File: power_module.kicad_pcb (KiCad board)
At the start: 4 copper layers, 95 x 66 mm, 71 parts, among them J1 USB_C_PD, J2 OUTPUT, J3 I2C_BREAKOUT, Q1 DUAL_N_FET, Q2 DUAL_N_FET, Q3 DUAL_N_FET, Q4 DUAL_N_FET, SW1 ON_OFF, U1 BQ7692003, U2 CH224K, U3 BQ24650, U4 LM5176PWPR

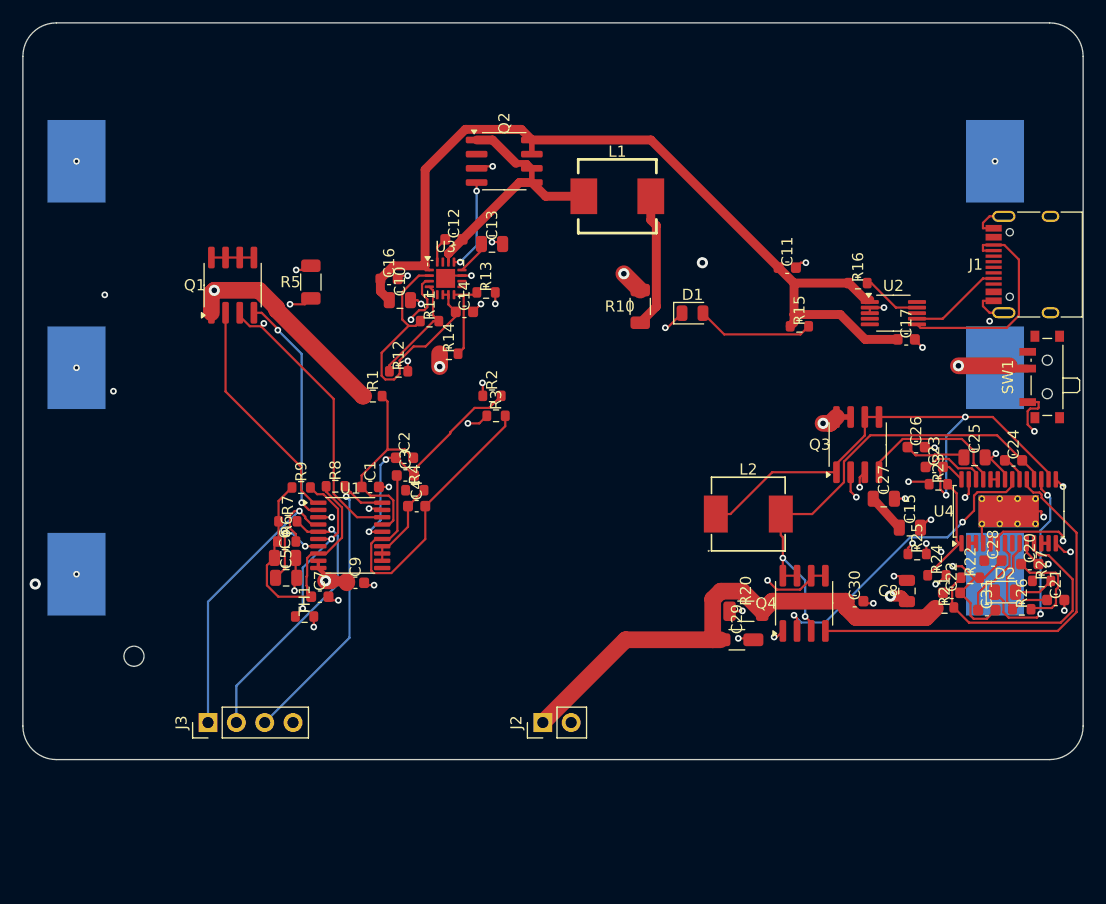
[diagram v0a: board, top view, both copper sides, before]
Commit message: Moved all the traces off GND layer, and some off PWR layer.
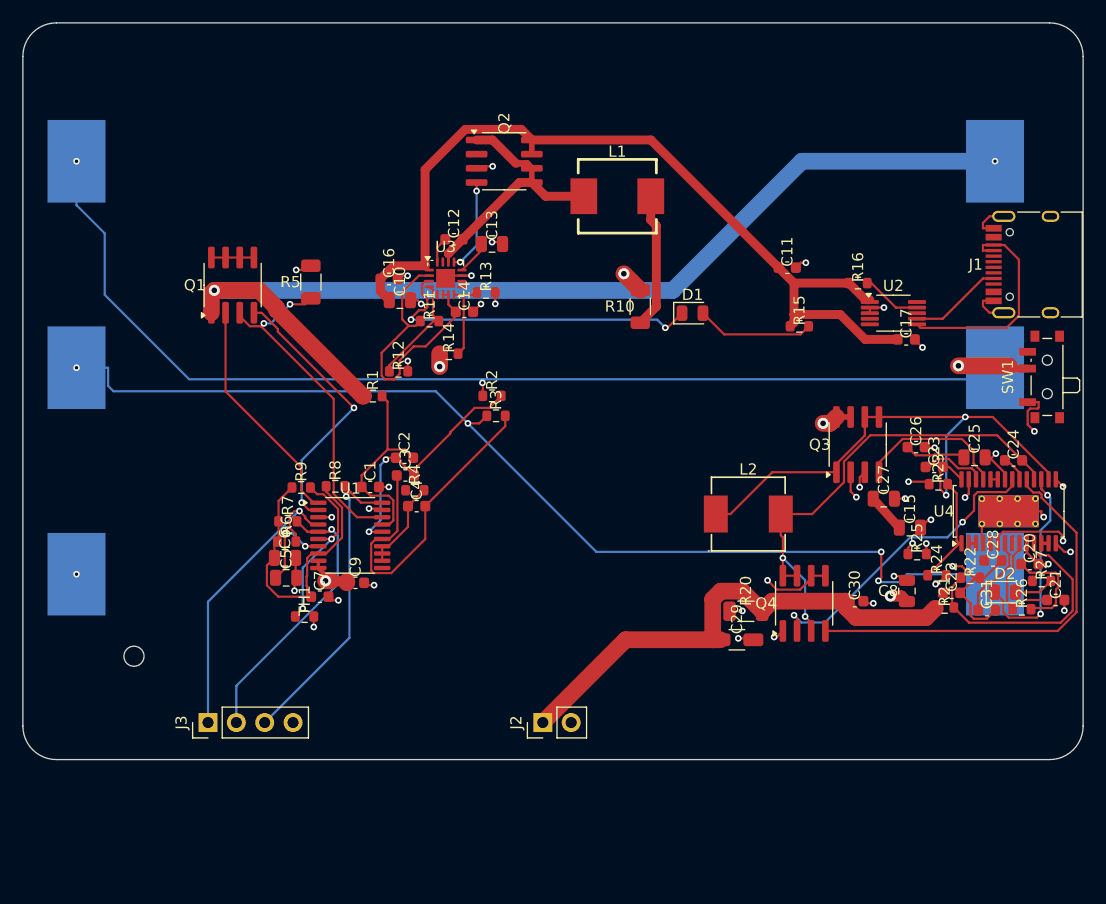
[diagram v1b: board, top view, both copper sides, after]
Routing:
- net CELL1_TOP: track 103.6 -> 97.8 mm, vias 4 -> 2
- net BAT+: track 26.7 -> 22.2 mm, vias 8 -> 7
- net BMS_CHG: track 21.0 -> 24.8 mm
- net CELL2_TOP: track 93.2 -> 95.4 mm
- net BAT-: vias 3 -> 2

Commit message: re-route attempt: DSN plane fix verified; pre-route on B.Cu
Three-pass re-route exercising yesterday's MCP fixes. Net change:

Attempt #1 (clean autoroute):
- planeLayersFlippedToPower: [In1.Cu, In2.Cu] confirmed the #203 fix
  is active. BAT+/BAT- now on F.Cu, not inner planes.
- Trade-off discovered: with inner layers locked, freerouting
  couldn't bridge the 82mm cell-holder span and left CELL1_TOP,
  CELL2_TOP entirely unrouted (65 unconnects).

Attempt #2 (pre-route + autoroute):
- 4 BAT1 trunks pre-routed on B.Cu at 1.5mm POWER_4A
  (CELL1_TOP, CELL2_TOP, BAT+, BAT- starter trunks).
- autoroute extended these into a full BAT+ F.Cu network
  through U3 and the decoupling caps. 442 tracks, 12 vias.
- 9 shorts remain — all at BAT1 pad 2 (CELL2_TOP) being
  crossed by U4's B.Cu signals (BB_SW1/SW2/PGOOD). This is the
  same structural issue as last session (different nets); BAT1.2
  sits inside U4's B.Cu envelope.

Mcp_expected_netclass_patterns bootstrapped on the .kicad_pro
(8 entries, no drift).

Board is NOT clean - committed for user review of the BAT1.2
issue and to checkpoint the strategy before tackling shorts.

See NOTES.md 2026-05-27 section for full details.
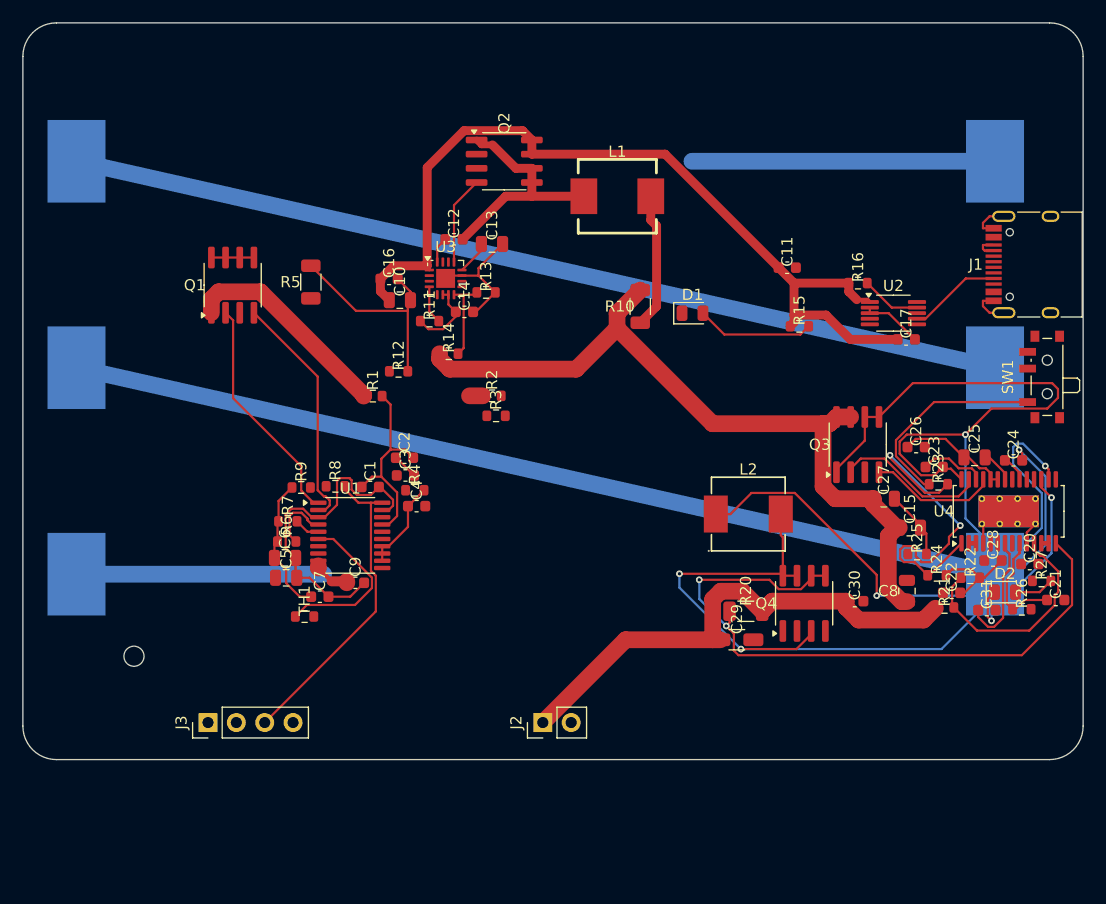
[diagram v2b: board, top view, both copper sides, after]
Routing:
- net BAT+: track 22.2 -> 96.1 mm, vias 7 -> 0
- net BB_SW1: track 50.2 -> 114.2 mm, vias 2 -> 3
- net BAT-: track 94.3 -> 46.2 mm, vias 2 -> 0
- net BB_HDRV2: track 37.3 -> 0.00 mm
- net SRP: track 31.0 -> 0.00 mm, vias 2 -> 0
- net BB_SW2: track 43.2 -> 74.1 mm, vias 2 -> 3
- net VC2: track 30.4 -> 0.00 mm
- net BQ_STAT1: track 30.1 -> 0.00 mm, vias 2 -> 0
- net BB_LDRV2: track 27.8 -> 0.00 mm, vias 2 -> 0
- net GND: track 71.1 -> 97.4 mm, vias 35 -> 0
- net SCL: track 24.9 -> 2.30 mm, vias 1 -> 0
- net SDA: track 28.2 -> 5.72 mm, vias 1 -> 0
- net BB_EN: track 9.98 -> 32.2 mm, vias 0 -> 2
- net BB_RT: track 22.2 -> 0.00 mm, vias 2 -> 0
- net VC1: track 22.5 -> 2.29 mm, vias 2 -> 0
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
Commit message: Moved U4 to bottom, away from pads and away from cells.  Swapped SMD thermistor for THT and moved to B.Cu.  Locked thermistor and BAT1.
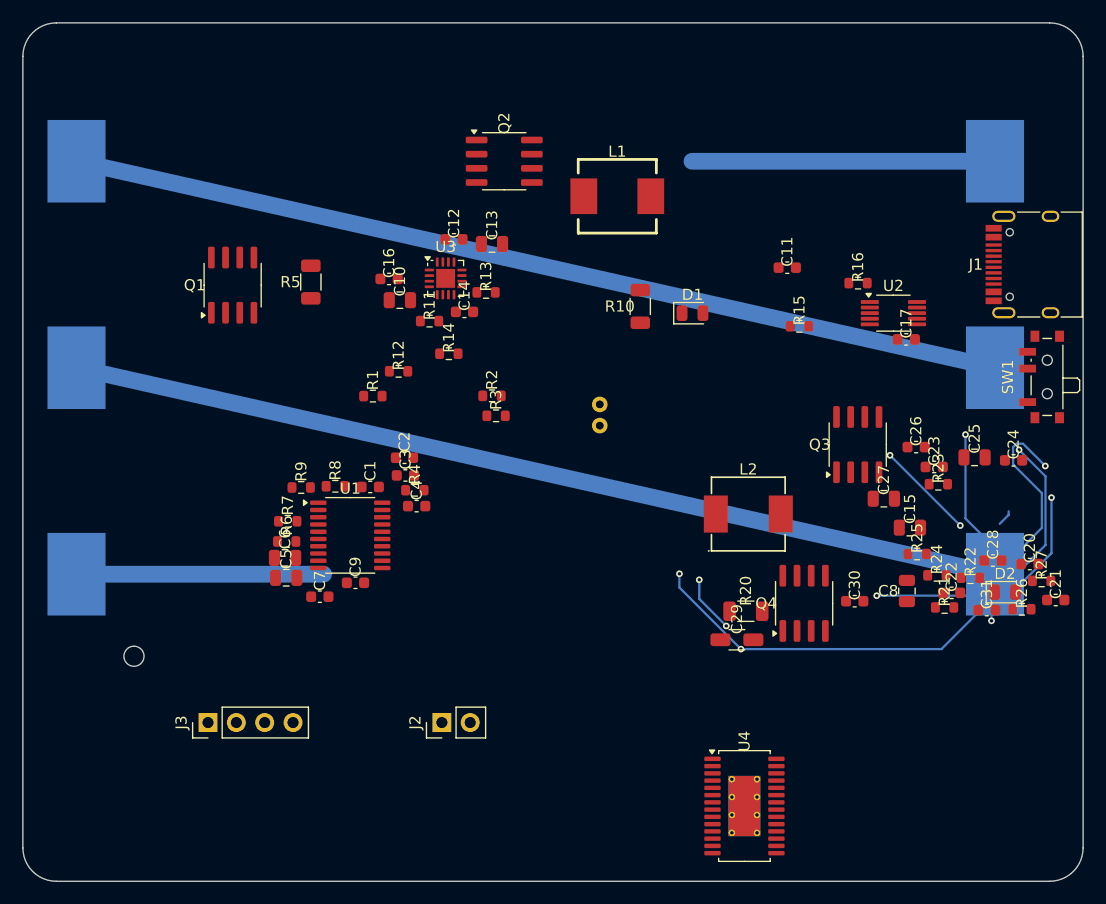
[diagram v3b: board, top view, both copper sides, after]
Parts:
- TH1: value NTC_10k -> 103AT NTC 10k +-3%; footprint Resistor_SMD:R_0603_1608Metric -> Resistor_THT:R_Axial_DIN0204_L3.6mm_D1.6mm_P1.90mm_Vertical; moved to B.Cu
- moved U4 35.5 mm to (64.7, 70.2), turned to 0 degrees
- moved TH1 31.5 mm to (51.7, 36.1), turned to 90 degrees
- moved J2 9.05 mm to (37.6, 62.7)
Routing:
- net BB_SW1: track 114.2 -> 0.00 mm, vias 3 -> 0
- net CELL2_TOP: track 84.4 -> 190.5 mm, vias 0 -> 8
- net GND: track 97.4 -> 1.46 mm
- net USB_VBUS: track 79.0 -> 0.00 mm
- net BB_SW2: track 74.1 -> 0.00 mm, vias 3 -> 0
- net BAT+: track 96.1 -> 22.1 mm
- net V12_INT: track 59.9 -> 5.14 mm
- net V12_OUT: track 46.2 -> 0.00 mm
- net ALERT: track 28.1 -> 0.00 mm
- net BB_EN: track 32.2 -> 8.90 mm
- net BMS_CHG: track 21.4 -> 0.00 mm
- net BQ_PH: track 21.0 -> 0.00 mm
- net BMS_DSG: track 20.7 -> 0.00 mm
- net BB_FB: track 20.6 -> 0.00 mm
- net BAT-: track 46.2 -> 27.2 mm
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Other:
- board size 95 x 66 mm -> 95 x 76.9 mm

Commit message: re-route with new U4 position: 0 shorts, 0 clearance
After U4 moved south (extending the board), re-ran the routing
pipeline: relax_placement → pre-route BAT1 trunks on B.Cu →
autoroute. Best result of the day at this checkpoint.

DRC: 65 errors / 106 warnings.
  - 0 shorts (the BAT1.2-in-U4-territory recurring issue is gone).
  - 0 clearance violations.
  - 9 track_width (pin-escape stubs - bridge candidates).
  - 53 unconnected (mostly GND pour-vias not added; #212 blocks).

Discovered MCP bug #212: stitch_pour_vias places vias only along
the zone outline boundary (skippedOutside=775), not the interior.
Zone.HitTest matches polygon edge, not containment.

64 of 71 components migrated south by relax_placement to follow U4.

See NOTES.md 2026-05-27 (second section) for details.
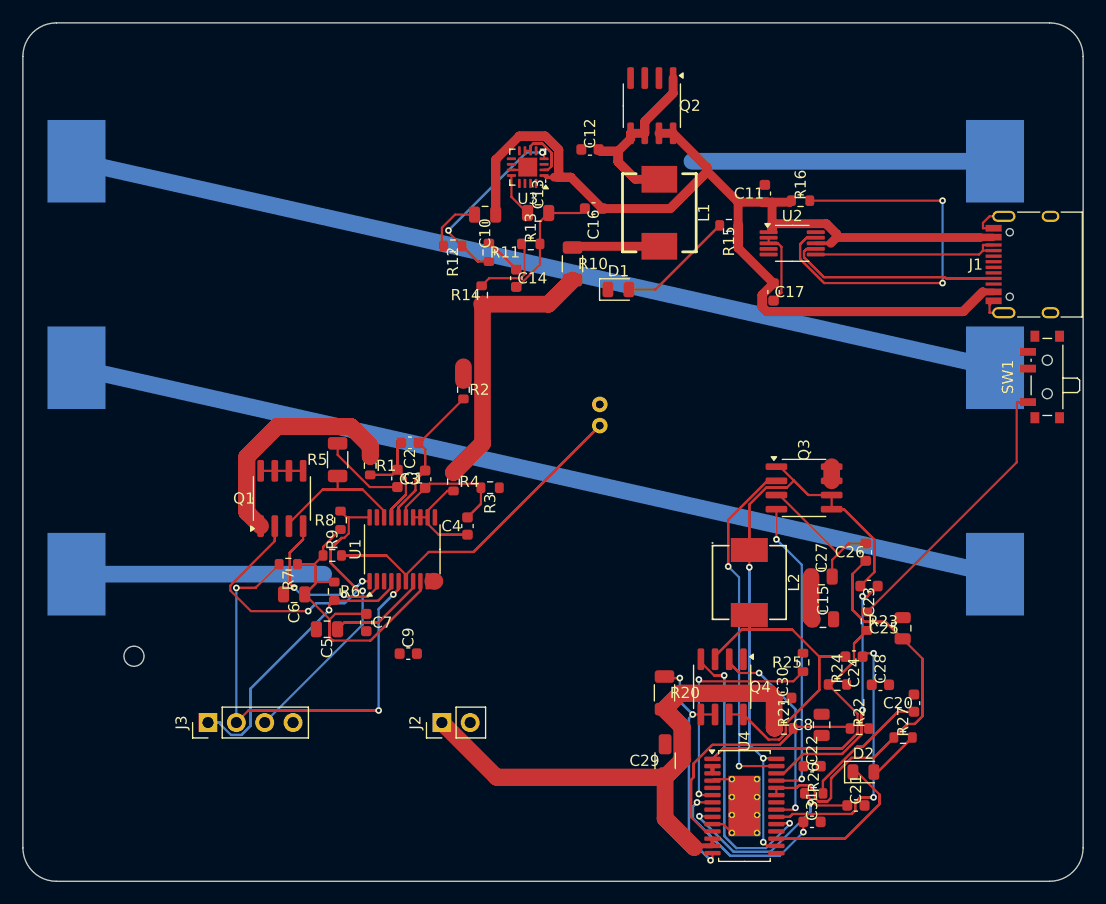
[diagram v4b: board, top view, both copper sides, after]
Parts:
- moved C21 25.7 mm to (74.7, 70.2)
- moved R26 24.9 mm to (70.9, 69.1)
- moved C31 24.6 mm to (70.8, 71.6)
- moved C24 22.7 mm to (74.5, 56.8), turned to 180 degrees
- moved D2 20.5 mm to (75.4, 67.2)
- moved C22 19.9 mm to (70.8, 66.6)
- moved Q1 19.6 mm to (23.3, 42.7)
- moved C16 19.4 mm to (51.2, 16.7), turned to 180 degrees
- moved R27 18.7 mm to (78.9, 64.1)
- moved R21 18.0 mm to (68.2, 63.3)
- moved R22 16.8 mm to (75.0, 63.3)
- moved C25 16.6 mm to (78.9, 54.3), turned to 90 degrees
- moved C20 16.2 mm to (79.9, 61.0), turned to 90 degrees
- moved R5 16.1 mm to (28.3, 39.2)
- moved C28 15.0 mm to (76.9, 59.4)
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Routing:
- net USB_VBUS: track 0.00 -> 150.1 mm
- net CELL2_TOP: track 190.5 -> 84.4 mm, vias 8 -> 0
- net V12_OUT: track 0.00 -> 90.2 mm
- net BB_SW1: track 0.00 -> 89.9 mm, vias 0 -> 3
- net BB_VCC: track 0.00 -> 67.6 mm
- net SCL: track 0.00 -> 58.2 mm, vias 0 -> 3
- net GND: track 1.46 -> 58.1 mm
- net TS1: track 0.00 -> 54.0 mm
- net BB_SW2: track 0.00 -> 51.9 mm
- net SDA: track 0.00 -> 48.1 mm, vias 0 -> 1
- net REGOUT: track 0.00 -> 46.7 mm
- net BB_HDRV2: track 0.00 -> 44.1 mm, vias 0 -> 2
- net CFG1: track 0.00 -> 41.9 mm, vias 0 -> 2
- net BB_HDRV1: track 0.00 -> 40.7 mm, vias 0 -> 2
- net BAT-: track 27.2 -> 66.5 mm
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
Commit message: apply via_orphan_pads + widen_return_paths: -15 DRC errors
via_orphan_pads added vias adjacent to:
  - 26 orphan F.Cu GND pads (skipped 30 already connected, 6 no
    clearance). Notable: 3 vias on U4 pin 29 (LM5176 thermal pad).
  - 2 orphan F.Cu BAT+ pads (C9.1, C8.1).

widen_return_paths widened 25 segments to 1.5 mm (POWER_4A width)
across 23 high-current components. 37 segments blocked by clearance
in the U4/U3/U1 thermal pad areas - those were skipped, no shorts
introduced.

Net: 65 -> 50 errors. Unconnects 51 -> 34 (17 closed). Still 0 shorts
and 0 clearance violations. 2 new tracks_crossing and 6 hole_to_hole
to clean up next pass.
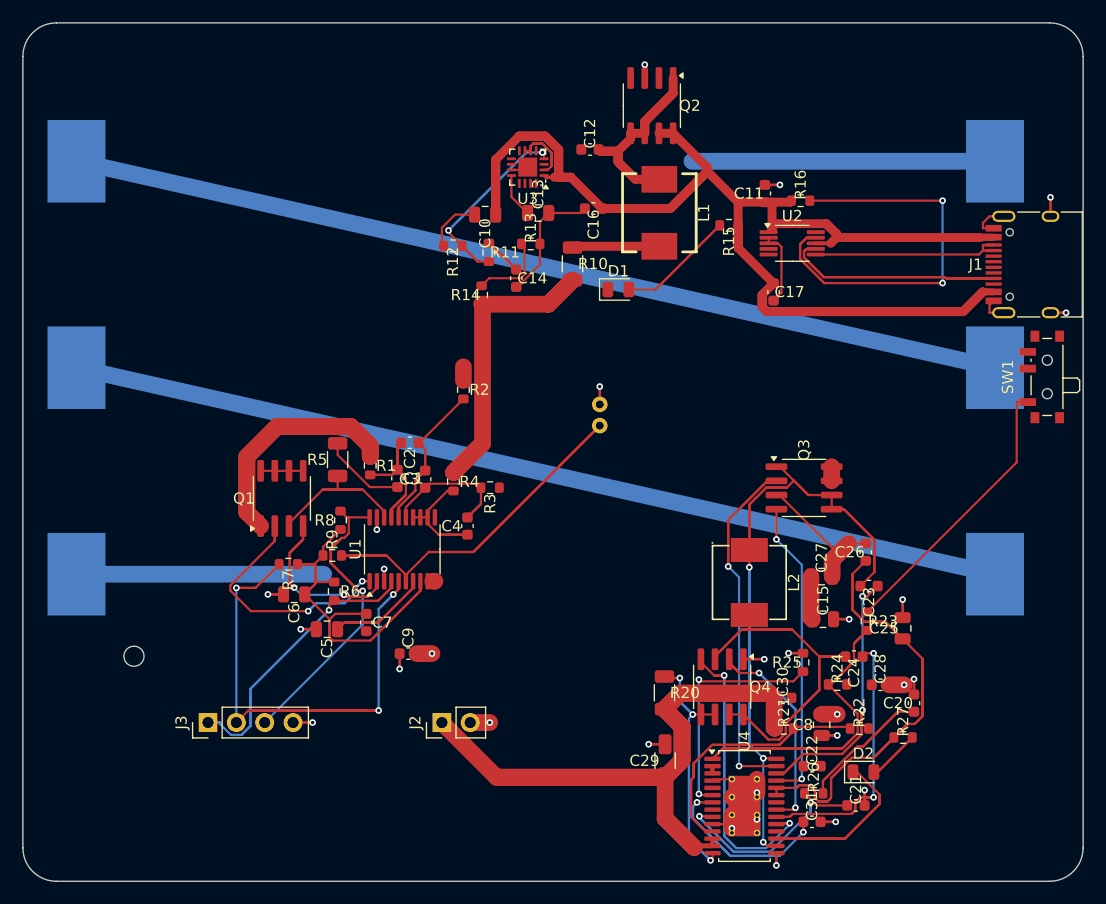
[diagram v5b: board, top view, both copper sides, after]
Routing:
- net GND: track 58.1 -> 94.4 mm, vias 0 -> 26
- net BAT+: track 60.5 -> 63.3 mm, vias 0 -> 2

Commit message: apply via_orphan_pads v3 + widen_return_paths: 65 -> 38 DRC errors
Re-applied the routing-finisher pipeline from the 574172e baseline
with the v2 + v3 toolchain:

via_orphan_pads v3 (orphan-chain detection + PTH/thermal-via skip
+ netclass-aware stub widths + stub-trace clearance check):
  - GND: 35 vias placed (skipped 4 already connected,
    8 no clearance — stub or via).
  - BAT+: 9 vias.
  - V12_OUT: 3 vias.

widen_return_paths: 19 GND/return stubs widened to 1.5 mm.

DRC: 65 -> 38 errors. Headline:
  - 0 shorts (vs v2's 8 - stub clearance v3 prevented every short).
  - 0 clearance violations.
  - 24-26 unconnects closed.
  - 11 track_width (mostly USB_VBUS pin-escape stubs, candidates
    for bridge_same_net_pins next pass).
  - 3 hole_to_hole (U4 thermal pad area - all redundant vias gone
    from v1, only inherent footprint hole-to-hole left).
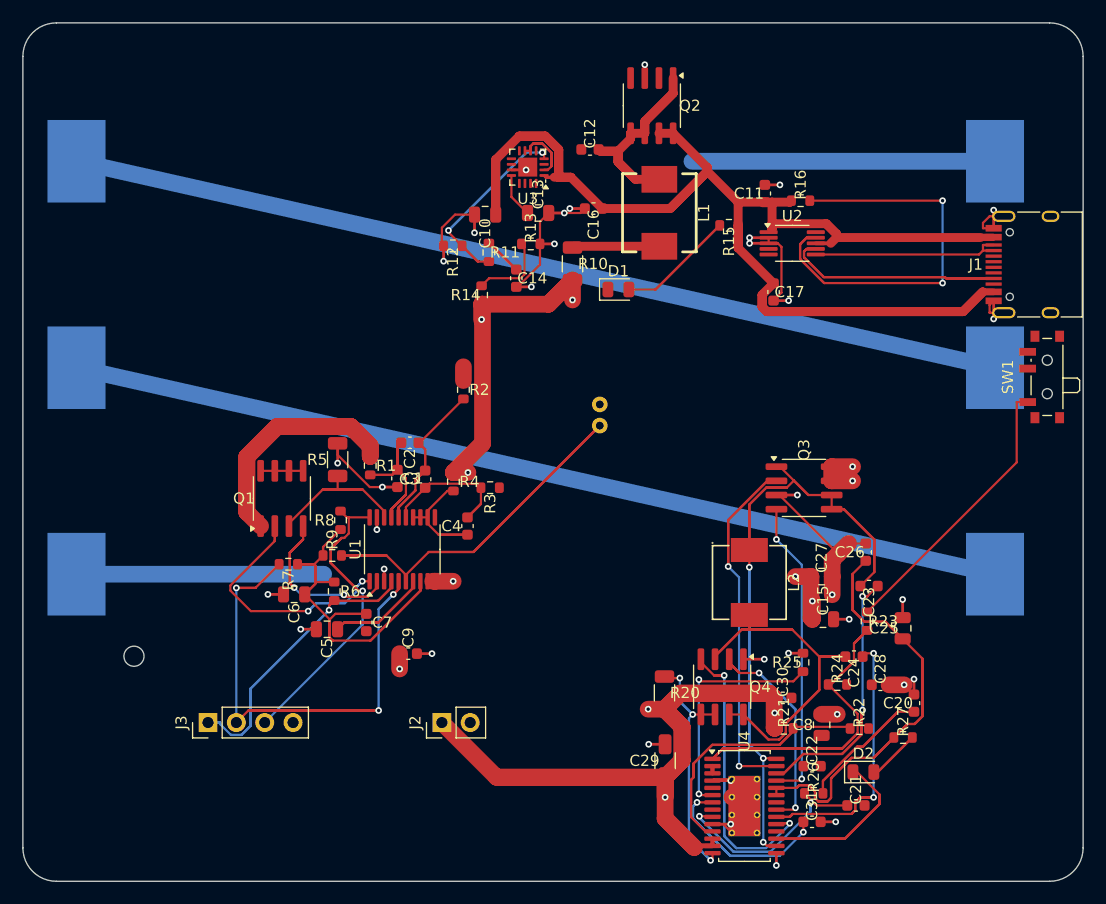
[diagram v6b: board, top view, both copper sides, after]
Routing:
- net GND: track 94.4 -> 108.9 mm, vias 26 -> 35
- net BAT+: track 63.3 -> 74.8 mm, vias 2 -> 9
- net V12_OUT: track 90.2 -> 94.8 mm, vias 0 -> 3
